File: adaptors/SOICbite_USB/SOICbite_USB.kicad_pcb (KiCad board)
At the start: 2 copper layers, 37.5 x 25 mm, 3 parts, among them J1 USB_B_Micro, J2 2x4_IDC, J3 Conn_01x05

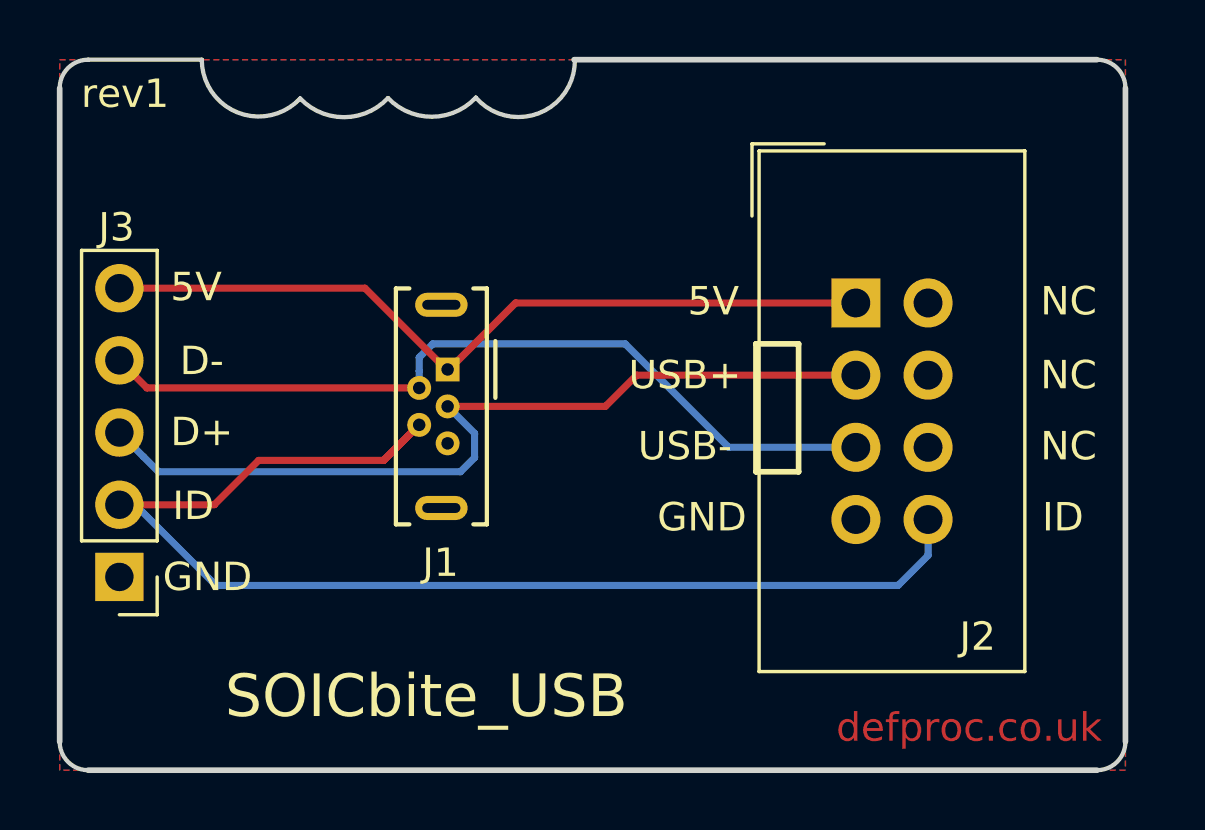
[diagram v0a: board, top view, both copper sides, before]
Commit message: rev2 layout, moved USB_ID to SOICbite pin 8
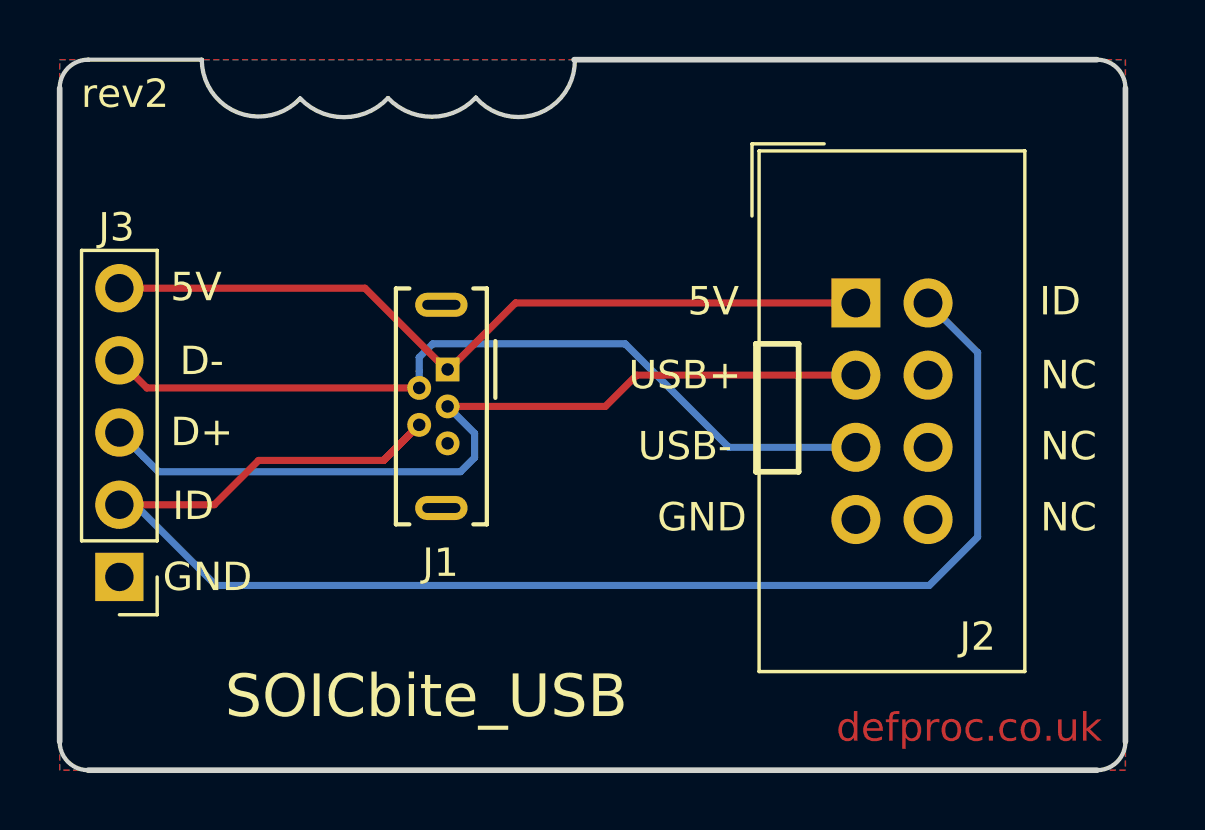
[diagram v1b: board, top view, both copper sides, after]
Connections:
- J2 pad 2: (no net) -> /USB_ID
- J2 pad 8: /USB_ID -> (no net)
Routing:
- net /USB_ID: track 44.8 -> 54.5 mm
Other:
- board text added: "rev2"
- board text removed: "rev1"
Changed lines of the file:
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@@
     (thickness 1.6)
     (drawings 33)
-    (tracks 34)
+    (tracks 35)
     (zones 0)
     (modules 3)
@@
     (pad 1 thru_hole rect (at 0 0) (size 1.7272 1.7272) (drill 1.016) (layers *.Cu *.Mask)
       (net 1 +5V))
-    (pad 2 thru_hole oval (at 2.54 0) (size 1.7272 1.7272) (drill 1.016) (layers *.Cu *.Mask))
+    (pad 2 thru_hole oval (at 2.54 0) (size 1.7272 1.7272) (drill 1.016) (layers *.Cu *.Mask)
+      (net 4 /USB_ID))
     (pad 3 thru_hole oval (at 0 2.54) (size 1.7272 1.7272) (drill 1.016) (layers *.Cu *.Mask)
       (net 3 /USB+))
@@
     (pad 7 thru_hole oval (at 0 7.62) (size 1.7272 1.7272) (drill 1.016) (layers *.Cu *.Mask)
       (net 5 GND))
-    (pad 8 thru_hole oval (at 2.54 7.62) (size 1.7272 1.7272) (drill 1.016) (layers *.Cu *.Mask)
-      (net 4 /USB_ID))
+    (pad 8 thru_hole oval (at 2.54 7.62) (size 1.7272 1.7272) (drill 1.016) (layers *.Cu *.Mask))
     (model ${KISYS3DMOD}/Connector_IDC.3dshapes/IDC-Header_2x04_P2.54mm_Vertical.wrl
       (at (xyz 0 0 0))
@@
     (effects (font (size 1 1) (thickness 0.2)))
   )
-  (gr_text NC (at 140.5 92) (layer F.SilkS)
+  (gr_text NC (at 140.5 99.6) (layer F.SilkS)
     (effects (font (size 1 1) (thickness 0.2)))
   )
@@
     (effects (font (size 1 1) (thickness 0.2)))
   )
-  (gr_text ID (at 140.3 99.6) (layer F.SilkS)
+  (gr_text ID (at 140.2 92) (layer F.SilkS)
     (effects (font (size 1 1) (thickness 0.2)))
   )
@@
     (effects (font (size 1 1) (thickness 0.2)))
   )
-  (gr_text rev1 (at 107.3 84.7) (layer F.SilkS)
+  (gr_text rev2 (at 107.3 84.7) (layer F.SilkS)
     (effects (font (size 1 1) (thickness 0.2)))
   )
@@
   (segment (start 107.1 99.16) (end 110.44 99.16) (width 0.25) (layer F.Cu) (net 4))
   (segment (start 110.44 99.16) (end 112 97.6) (width 0.25) (layer F.Cu) (net 4))
+  (segment (start 110.5 102) (end 107.66 99.16) (width 0.25) (layer B.Cu) (net 4))
+  (segment (start 137.3 100.3) (end 135.6 102) (width 0.25) (layer B.Cu) (net 4))
   (segment (start 107.66 99.16) (end 107.1 99.16) (width 0.25) (layer B.Cu) (net 4))
-  (segment (start 135.555001 99.680001) (end 135.555001 100.944999) (width 0.25) (layer B.Cu) (net 4))
-  (segment (start 110.5 102) (end 107.66 99.16) (width 0.25) (layer B.Cu) (net 4))
-  (segment (start 134.5 102) (end 110.5 102) (width 0.25) (layer B.Cu) (net 4))
-  (segment (start 135.555001 100.944999) (end 134.5 102) (width 0.25) (layer B.Cu) (net 4))
+  (segment (start 135.6 102) (end 110.5 102) (width 0.25) (layer B.Cu) (net 4))
+  (segment (start 135.555001 92.060001) (end 137.3 93.805) (width 0.25) (layer B.Cu) (net 4))
+  (segment (start 137.3 93.805) (end 137.3 100.3) (width 0.25) (layer B.Cu) (net 4))
   (zone (net 5) (net_name GND) (layer F.Cu) (hatch edge 0.508)
     (connect_pads (clearance 0.254))

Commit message: revised pinout, D- should be by Vcc
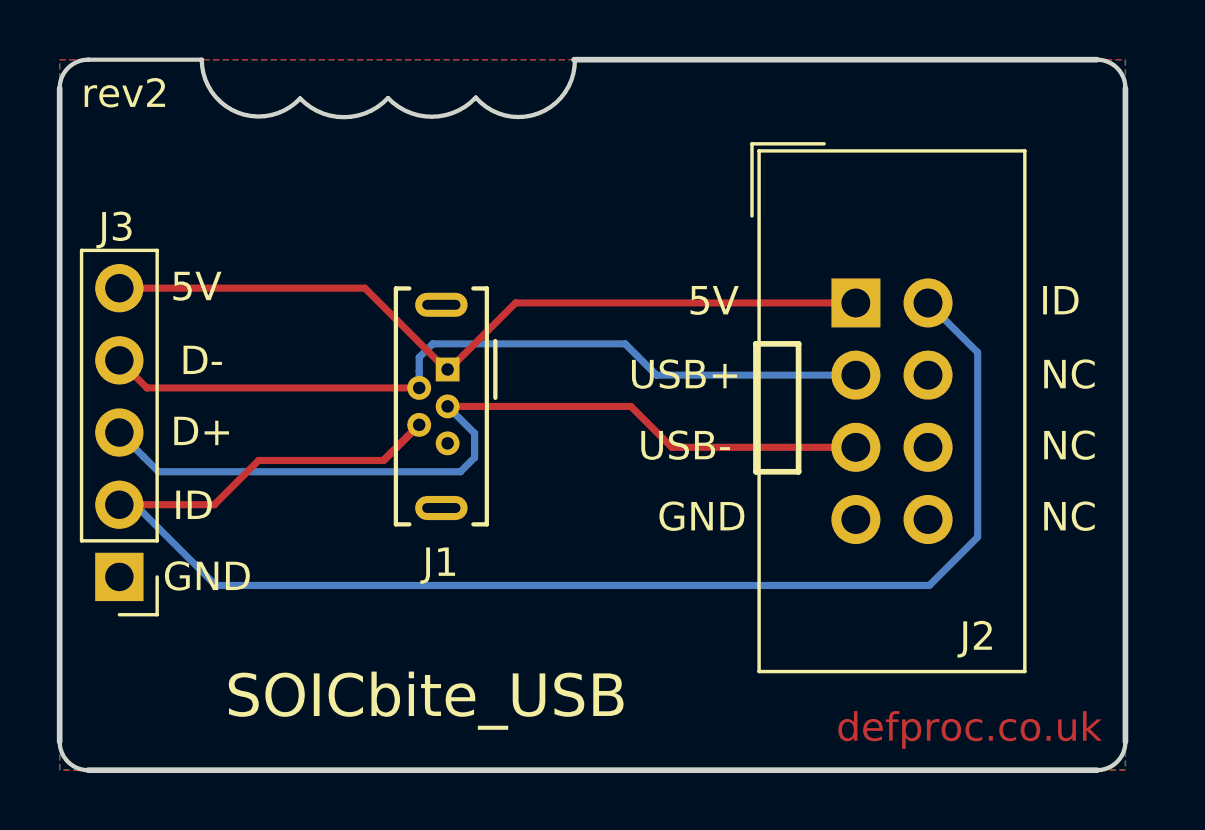
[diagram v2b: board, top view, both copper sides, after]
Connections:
- J2 pad 3: /USB+ -> /USB-
- J2 pad 5: /USB- -> /USB+
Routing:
- net /USB-: track 29.1 -> 28.0 mm
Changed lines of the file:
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@@
       (net 4 /USB_ID))
     (pad 3 thru_hole oval (at 0 2.54) (size 1.7272 1.7272) (drill 1.016) (layers *.Cu *.Mask)
-      (net 3 /USB+))
+      (net 2 /USB-))
     (pad 4 thru_hole oval (at 2.54 2.54) (size 1.7272 1.7272) (drill 1.016) (layers *.Cu *.Mask))
     (pad 5 thru_hole oval (at 0 5.08) (size 1.7272 1.7272) (drill 1.016) (layers *.Cu *.Mask)
-      (net 2 /USB-))
+      (net 3 /USB+))
     (pad 6 thru_hole oval (at 2.54 5.08) (size 1.7272 1.7272) (drill 1.016) (layers *.Cu *.Mask))
     (pad 7 thru_hole oval (at 0 7.62) (size 1.7272 1.7272) (drill 1.016) (layers *.Cu *.Mask)
@@
   (segment (start 124.9 93.5) (end 118.124998 93.5) (width 0.25) (layer B.Cu) (net 2))
   (segment (start 117.65 94.456031) (end 117.65 95.05) (width 0.25) (layer B.Cu) (net 2))
-  (segment (start 133.015001 97.140001) (end 128.540001 97.140001) (width 0.25) (layer B.Cu) (net 2))
-  (segment (start 128.540001 97.140001) (end 124.9 93.5) (width 0.25) (layer B.Cu) (net 2))
-  (segment (start 124.2 95.7) (end 118.65 95.7) (width 0.25) (layer F.Cu) (net 3))
-  (segment (start 133.015001 94.600001) (end 125.299999 94.600001) (width 0.25) (layer F.Cu) (net 3))
-  (segment (start 125.299999 94.600001) (end 124.2 95.7) (width 0.25) (layer F.Cu) (net 3))
+  (segment (start 133.015001 94.600001) (end 126.000001 94.600001) (width 0.25) (layer B.Cu) (net 2))
+  (segment (start 126.000001 94.600001) (end 124.9 93.5) (width 0.25) (layer B.Cu) (net 2))
   (segment (start 107.949999 97.469999) (end 107.1 96.62) (width 0.25) (layer B.Cu) (net 3))
   (segment (start 108.48 98) (end 107.949999 97.469999) (width 0.25) (layer B.Cu) (net 3))
@@
   (segment (start 118.65 95.7) (end 119.6 96.65) (width 0.25) (layer B.Cu) (net 3))
   (segment (start 119.6 96.65) (end 119.6 97.5) (width 0.25) (layer B.Cu) (net 3))
+  (segment (start 125.1 95.7) (end 118.65 95.7) (width 0.25) (layer F.Cu) (net 3))
+  (segment (start 133.015001 97.140001) (end 126.540001 97.140001) (width 0.25) (layer F.Cu) (net 3))
+  (segment (start 126.540001 97.140001) (end 125.1 95.7) (width 0.25) (layer F.Cu) (net 3))
   (segment (start 117.230001 96.769999) (end 117.65 96.35) (width 0.25) (layer F.Cu) (net 4))
   (segment (start 116.4 97.6) (end 117.230001 96.769999) (width 0.25) (layer F.Cu) (net 4))

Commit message: and update the silkscreen to match the D+/D- swap
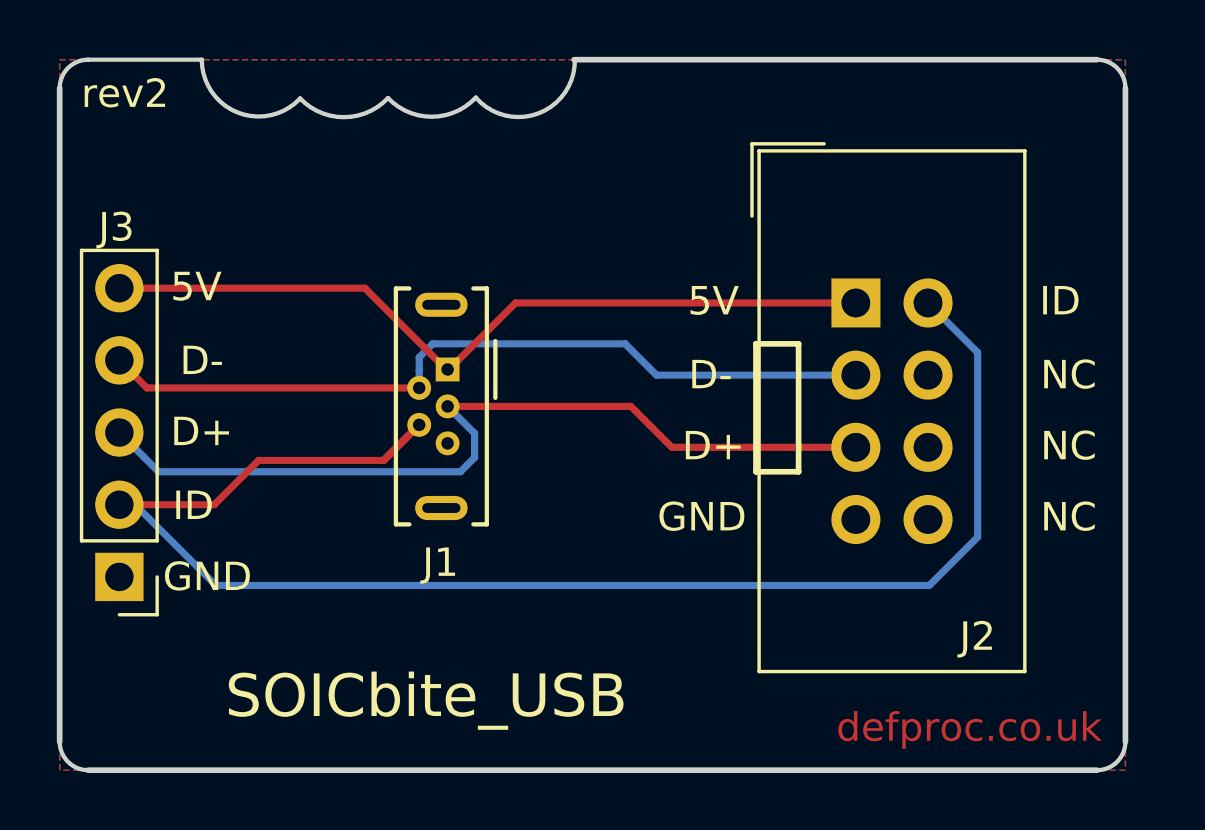
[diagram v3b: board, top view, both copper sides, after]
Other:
- board text removed: "USB+"
- board text removed: "USB-"
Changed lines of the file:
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@@
     (effects (font (size 1 1) (thickness 0.2)))
   )
-  (gr_text USB- (at 127 97.1) (layer F.SilkS)
+  (gr_text D+ (at 128 97.1) (layer F.SilkS)
     (effects (font (size 1 1) (thickness 0.2)))
   )
-  (gr_text USB+ (at 127 94.6) (layer F.SilkS)
+  (gr_text D- (at 127.9 94.6) (layer F.SilkS)
     (effects (font (size 1 1) (thickness 0.2)))
   )
